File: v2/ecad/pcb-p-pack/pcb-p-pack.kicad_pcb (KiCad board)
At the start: 2 copper layers, 70 x 44 mm, 60 parts, among them Q1 CSD17570Q5B 30 V N-FET, charg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, Q2 CSD17570Q5B 30 V N-FET, disch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, U1 BQ4050RSMR: SMBus 1.1 gas gau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

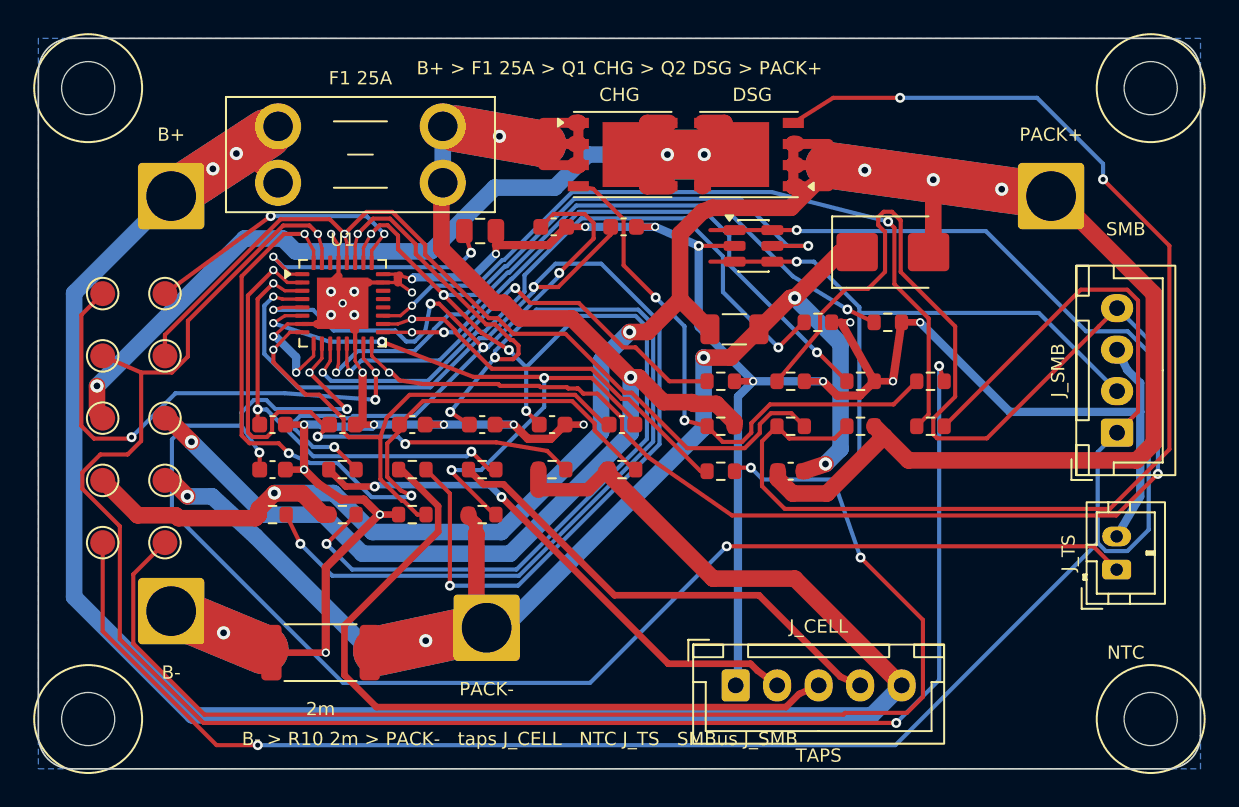
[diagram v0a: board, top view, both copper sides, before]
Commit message: feat(pcb-p): P2 routed clean under the full gate set (0 hard, 0 open, three rails MET, contracts pass): the ground stitch grid on the underside pour, the 0.5 mm power class for the sense links, the intent's current sinks; deliverable meshsat-pcb-p-revA-P2 [MESHSAT-862]
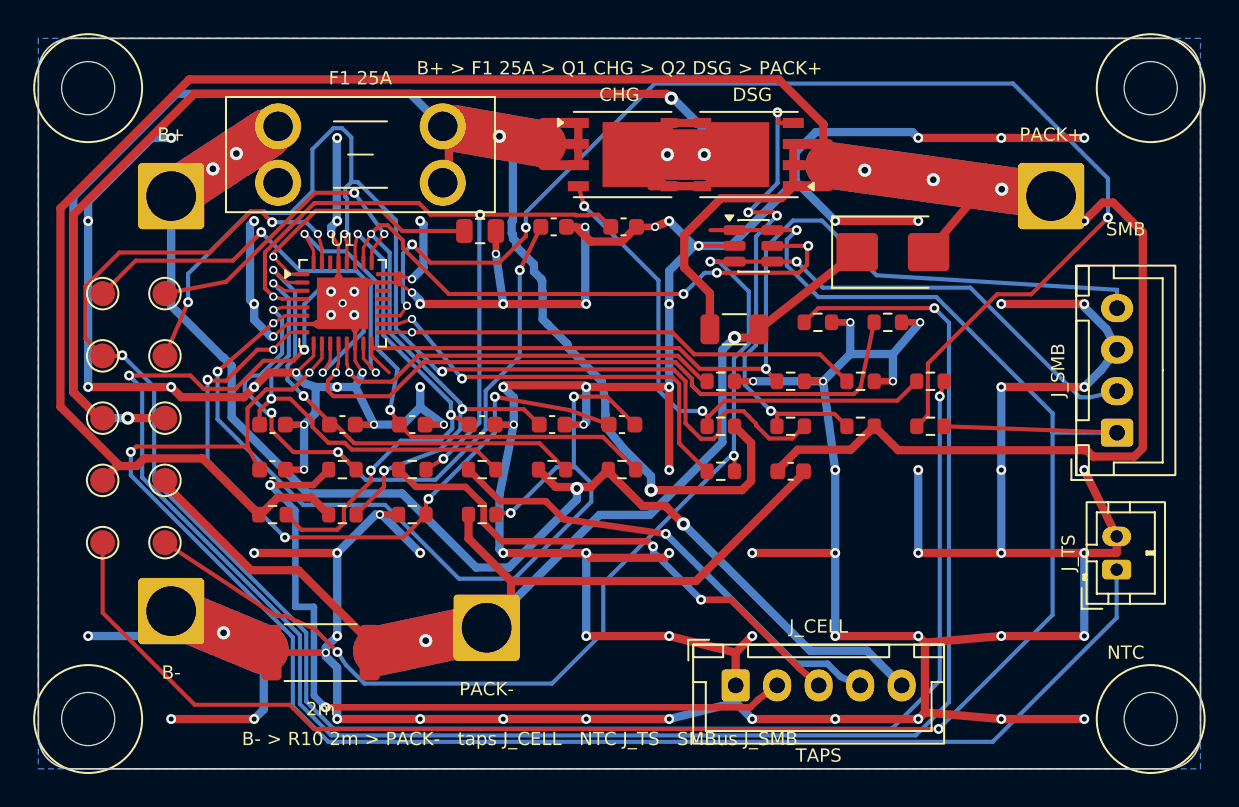
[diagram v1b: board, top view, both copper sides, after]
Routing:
- net GND: track 187.7 -> 445.5 mm, vias 29 -> 95
- net /TS2: track 40.8 -> 123.9 mm, vias 2 -> 4
- net /PRES: track 108.5 -> 59.1 mm, vias 2 -> 1
- net /DSG_G: track 75.0 -> 29.0 mm, vias 2 -> 4
- net /CELL4: track 127.0 -> 87.9 mm, vias 2 -> 4
- net /PACK_F: track 68.8 -> 30.9 mm, vias 4 -> 3
- net /PACK_P: track 150.4 -> 184.1 mm, vias 5 -> 4
- net /SMBD: track 116.5 -> 86.8 mm, vias 3 -> 4
- net /SMBC_I: track 47.3 -> 76.7 mm, vias 2 -> 4
- net /VC2_F: track 72.3 -> 44.2 mm
- net /SMBC: track 148.1 -> 120.9 mm
- net /VCC_F: track 88.1 -> 62.2 mm
- net /BAT_F: track 50.1 -> 32.1 mm, vias 3 -> 2
- net /DSG_R: track 53.1 -> 69.7 mm, vias 1 -> 3
- net /SRN_F: track 38.3 -> 54.7 mm
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
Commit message: fix(release): P2 retitled from P1 on its silk and its deliverable rebuilt, the first to pass all 35 properties of verify_deliverable (it had lost meshsat.pretty and the full BOM to the copy bug) [MESHSAT-862]
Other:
- board text added: "PCB-P PACK BMS REV A (P2)"
- board text removed: "PCB-P PACK BMS REV A (P1)"
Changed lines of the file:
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@@
 		)
 	)
-	(gr_text "PCB-P PACK BMS REV A (P1)"
+	(gr_text "PCB-P PACK BMS REV A (P2)"
 		(at 100 103 0)
 		(layer "B.SilkS")

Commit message: feat(ecad): P3 released, the pack BMS with the decoupling floor plan; 0 hard, 0 unrouted, 36 of 36 deliverable properties [MESHSAT-862]
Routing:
- net /PACK_P: track 184.1 -> 124.2 mm, vias 4 -> 6
- net /DSG_R: track 69.7 -> 121.4 mm, vias 3 -> 4
- net /BAT_F: track 32.1 -> 79.1 mm, vias 2 -> 4
- net /SMBC_I: track 76.7 -> 38.0 mm, vias 4 -> 2
- net /TS2: track 123.9 -> 86.1 mm, vias 4 -> 2
- net /PACK_N: track 93.8 -> 120.1 mm, vias 2 -> 6
- net /SMBC: track 120.9 -> 94.9 mm, vias 2 -> 1
- net /SRN_F: track 54.7 -> 31.4 mm, vias 4 -> 2
- net /VC4_F: track 28.5 -> 50.3 mm, vias 2 -> 3
- net /SMBD: track 86.8 -> 104.3 mm, vias 4 -> 1
- net /CELL1: track 47.0 -> 32.3 mm
- net /PACK_F: track 30.9 -> 44.5 mm, vias 3 -> 2
- net /VC2_F: track 44.2 -> 57.7 mm, vias 3 -> 5
- net /PRES: track 59.1 -> 48.3 mm
- net /VC3_F: track 27.0 -> 37.2 mm, vias 2 -> 4
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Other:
- board text added: "PCB-P PACK BMS REV A (P3)"
- board text removed: "PCB-P PACK BMS REV A (P2)"
